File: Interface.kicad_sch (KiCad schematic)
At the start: 32 parts, among them J5601 VBUS_1, J5602 VBUS_2, J5901 SPI, J5902 UART, J5903 Battery_1, J5904 Battery_2, J5905 PV_1, J5906 PV_2, J5907 PV_3, J5908 PV_4, J5909 CH_O_1, J5910 CH_O_2, J5911 CH_O_3, J5912 CH_O_4, J5913 CH_O_5, J5914 CH_O_6, J5915 PV_5, J5916 PV_6, J5917 CH_5V_1, J5918 CH_5V_2, J5919 CH_12V_1, J5920 CH_12V_2

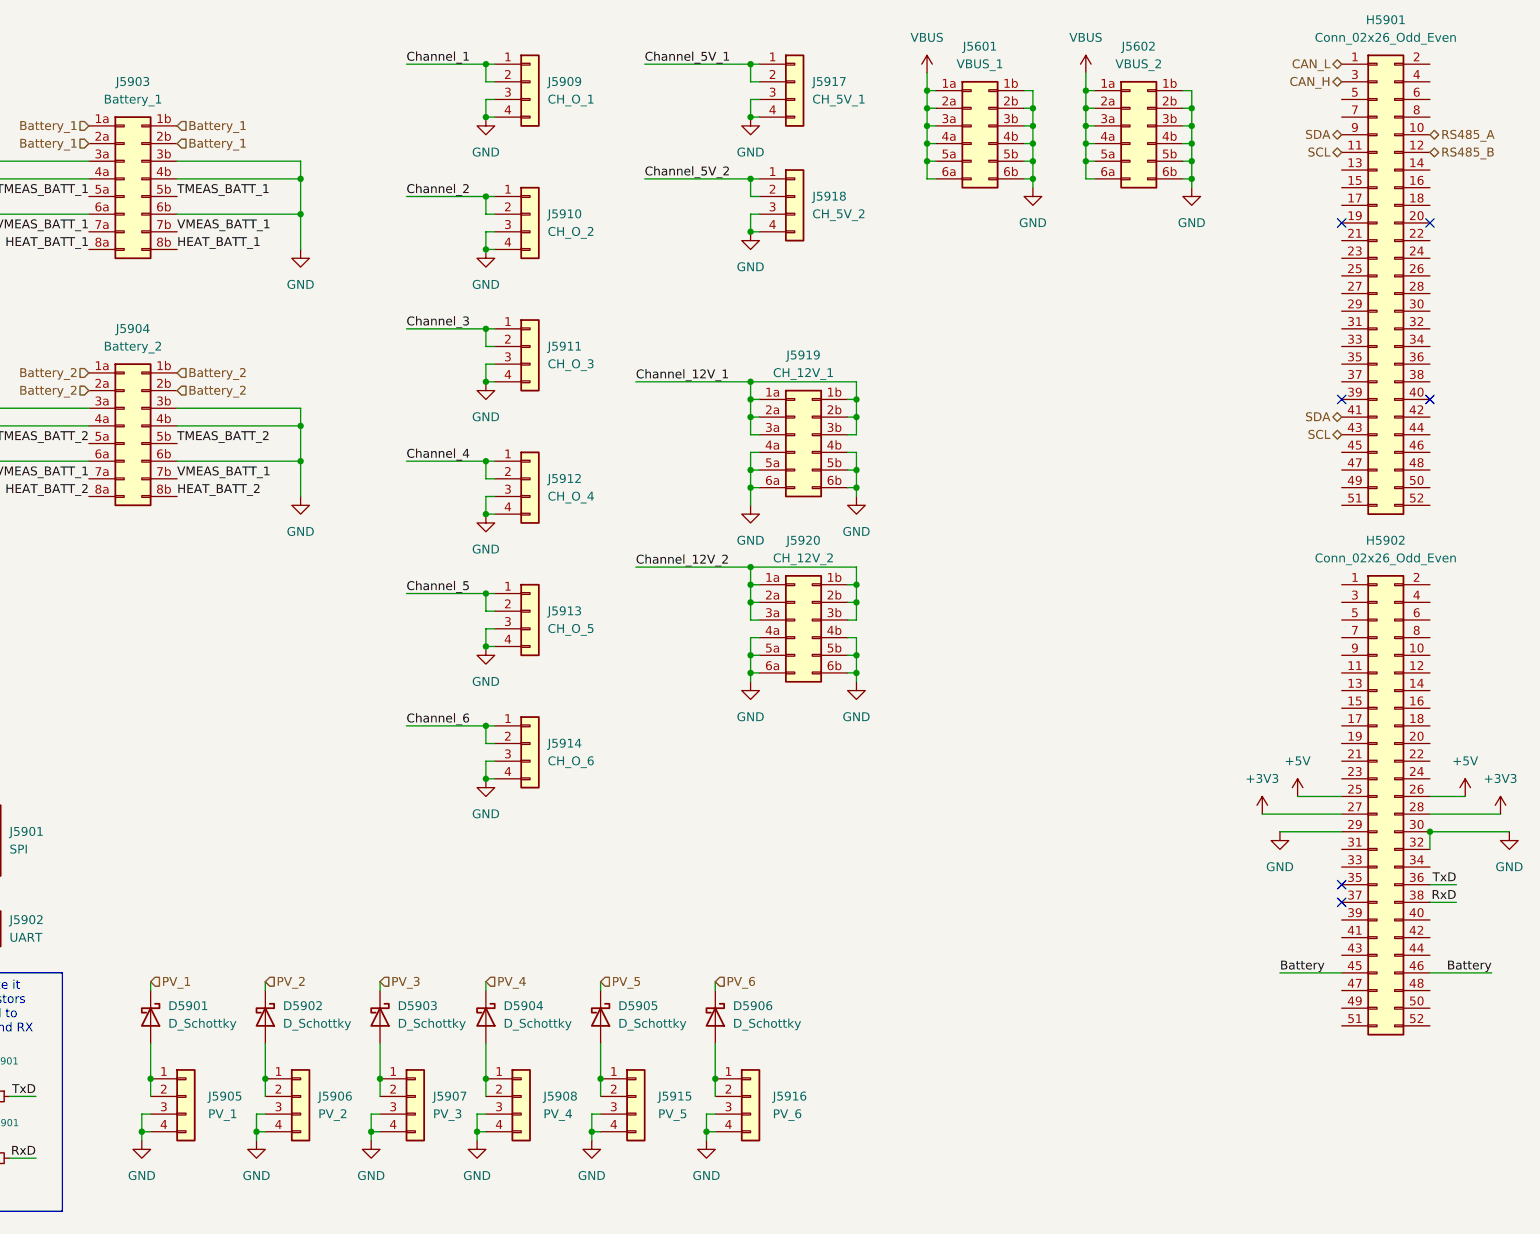
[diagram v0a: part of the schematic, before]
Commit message: added second AMUX and housekeeping
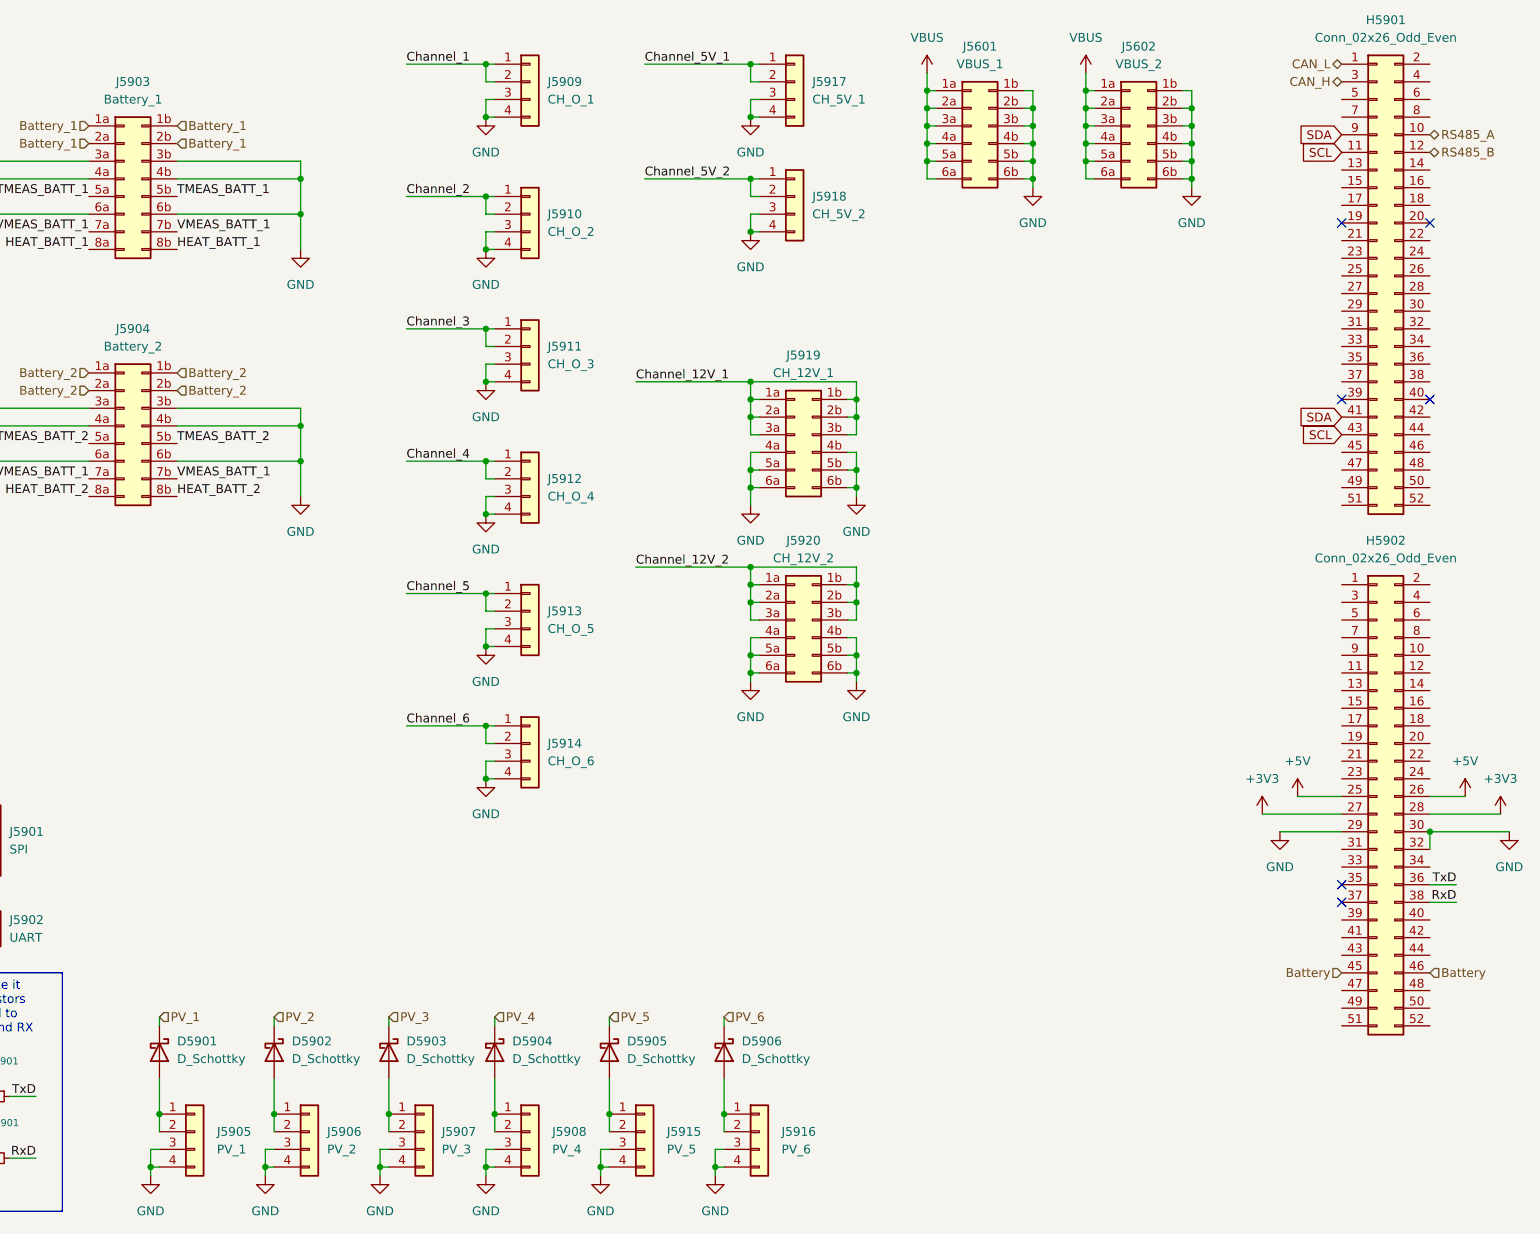
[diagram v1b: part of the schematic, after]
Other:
- moved on the sheet: D5901, D5902, D5903, D5904, D5905, D5906, J5905, J5906, J5907, J5908, J5915, J5916

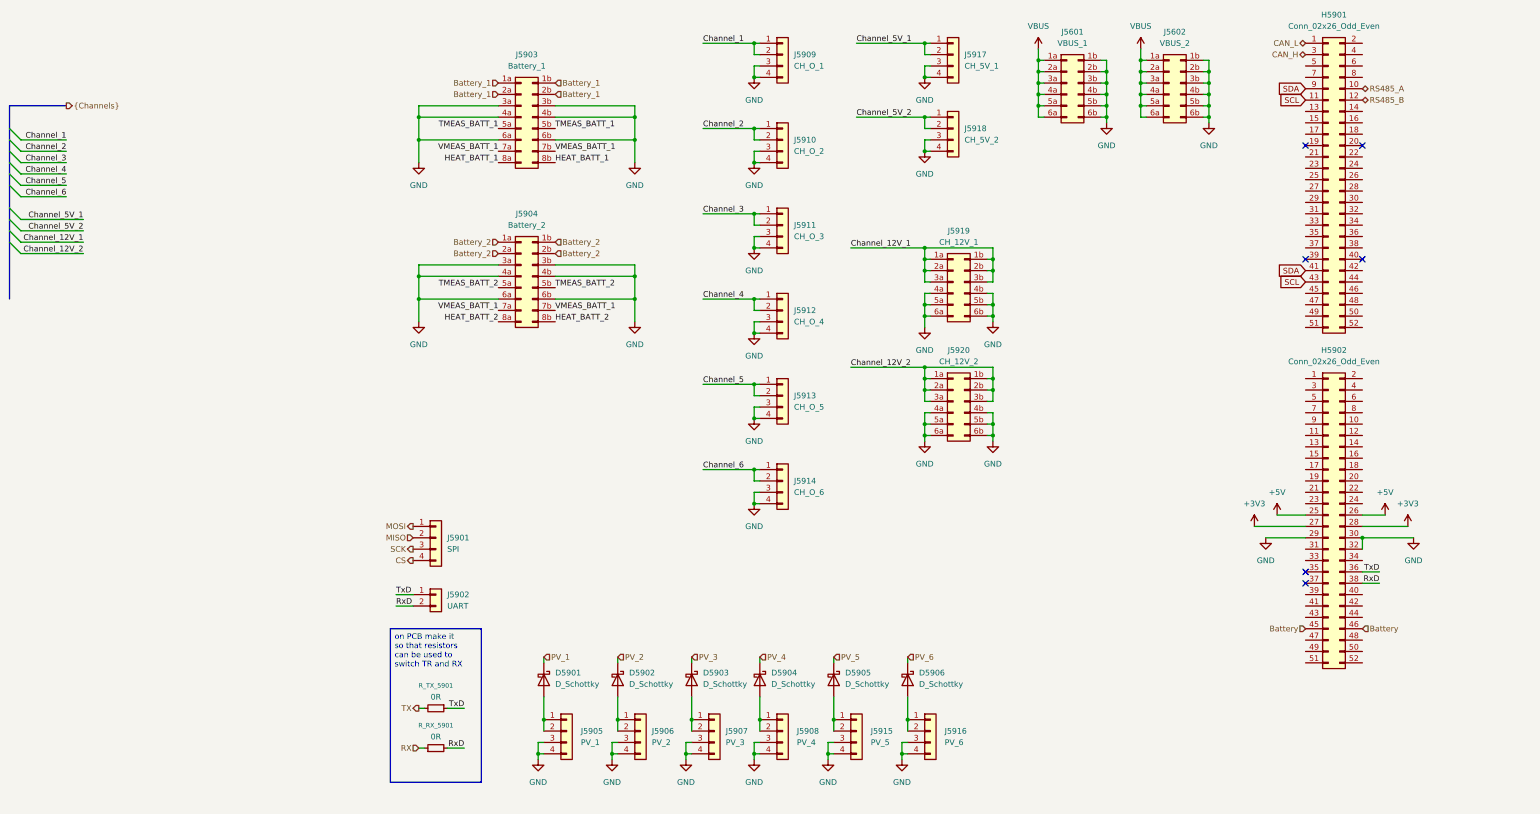
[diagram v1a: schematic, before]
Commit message: added RS422, housekeeping
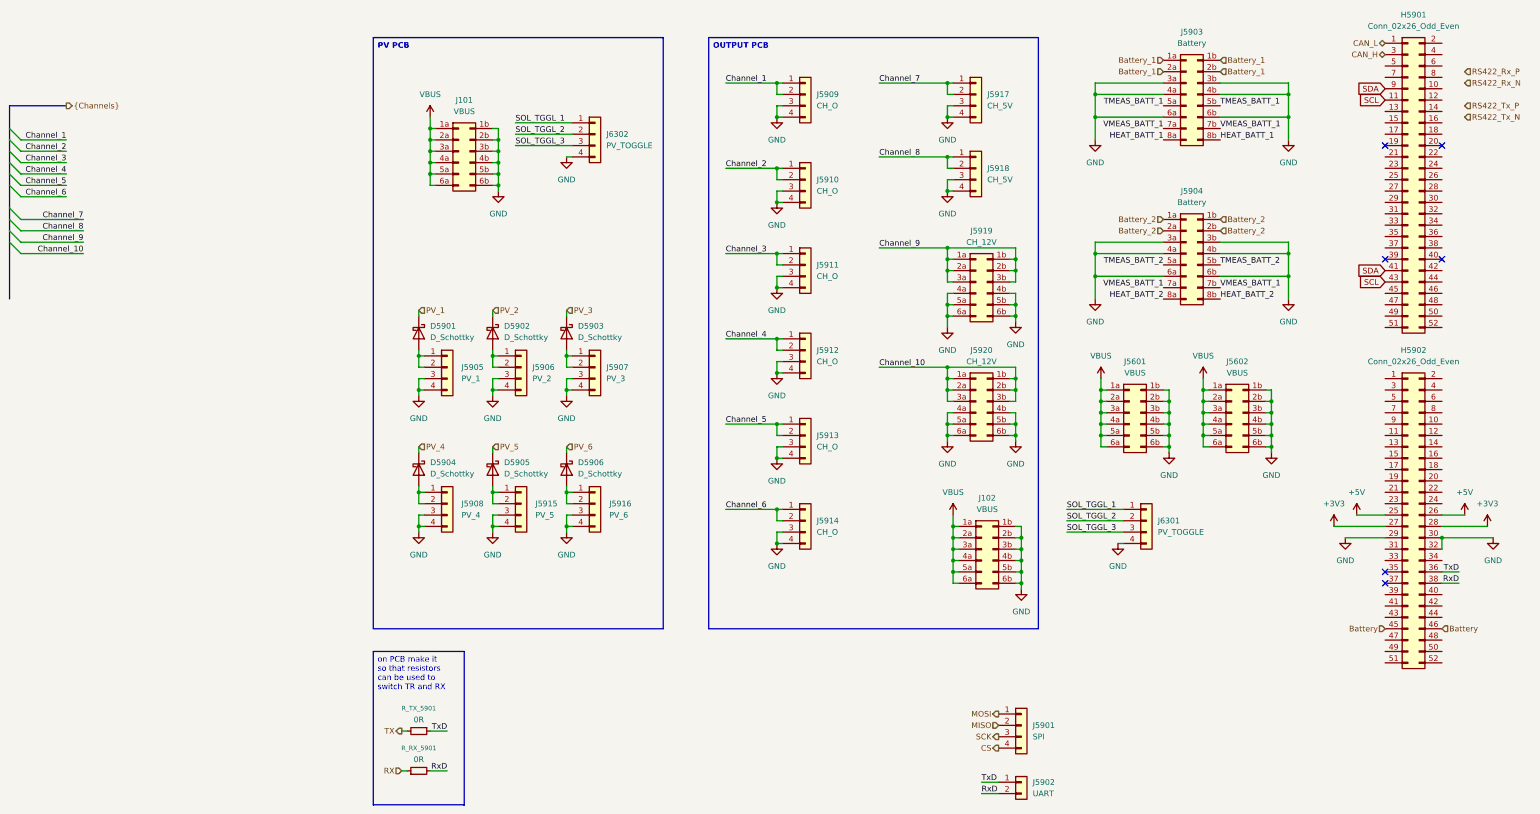
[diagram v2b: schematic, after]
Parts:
- added J101, J102: VBUS, symbol Connector_Generic:Conn_02x06_Row_Letter_Last
- added J6301, J6302: PV_TOGGLE, Connector_Molex:Molex_CLIK-Mate_502494-0470_1x04-1MP_P2.00mm_Horizontal, symbol Connector_Generic:Conn_01x04
- J5601: value VBUS_1 -> VBUS
- J5602: value VBUS_2 -> VBUS
- J5903: value Battery_1 -> Battery
- J5904: value Battery_2 -> Battery
- J5909: value CH_O_1 -> CH_O
- J5910: value CH_O_2 -> CH_O
- J5911: value CH_O_3 -> CH_O
- J5912: value CH_O_4 -> CH_O
- J5913: value CH_O_5 -> CH_O
- J5914: value CH_O_6 -> CH_O
- J5917: value CH_5V_1 -> CH_5V
- J5918: value CH_5V_2 -> CH_5V
- J5919: value CH_12V_1 -> CH_12V
- J5920: value CH_12V_2 -> CH_12V
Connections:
- net GND: now also J101.1b (Pin_1b), J101.2b (Pin_2b), J101.3b (Pin_3b), J101.4b (Pin_4b), J101.5b (Pin_5b), J101.6b (Pin_6b), J102.1b (Pin_1b), J102.2b (Pin_2b), J102.3b (Pin_3b), J102.4b (Pin_4b), J102.5b (Pin_5b), J102.6b (Pin_6b), J6301.4 (Pin_4), J6302.4 (Pin_4)
- net VBUS: now also J101.1a (Pin_1a), J101.2a (Pin_2a), J101.3a (Pin_3a), J101.4a (Pin_4a), J101.5a (Pin_5a), J101.6a (Pin_6a), J102.1a (Pin_1a), J102.2a (Pin_2a), J102.3a (Pin_3a), J102.4a (Pin_4a), J102.5a (Pin_5a), J102.6a (Pin_6a)
- net Channel_12V_1 renamed Channel_9
- net Channel_12V_2 renamed Channel_10
- net Channel_5V_1 renamed Channel_7
- net Channel_5V_2 renamed Channel_8
- net RS485_A: no longer names the net of H5901.10 (Pin_10)
- net RS485_B: no longer names the net of H5901.12 (Pin_12)
- new net SOL_TGGL_1: J6301.1 (Pin_1), J6302.1 (Pin_1)
- new net SOL_TGGL_2: J6301.2 (Pin_2), J6302.2 (Pin_2)
- new net SOL_TGGL_3: J6301.3 (Pin_3), J6302.3 (Pin_3)
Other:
- moved on the sheet: D5901, D5902, D5903, D5904, D5905, D5906, H5901, H5902, J5601, J5602, J5901, J5902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

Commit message: updated battery pack module; updated solar inputs module
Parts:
- removed J6301, J6302: PV_TOGGLE, Connector_Molex:Molex_CLIK-Mate_502494-0470_1x04-1MP_P2.00mm_Horizontal, symbol Connector_Generic:Conn_01x04
- added H6301, H6302, H6303, H6304: PC104, Connector_PinSocket_2.54mm:PinSocket_2x26_P2.54mm_Vertical, symbol Connector_Generic:Conn_02x26_Odd_Even
- added J6322: HEADER_PV, Connector_PinSocket_2.54mm:PinSocket_1x08_P2.54mm_Vertical, symbol Connector:Conn_01x08_Socket
- added J6323: HEADER_PV, Connector_PinHeader_2.54mm:PinHeader_1x08_P2.54mm_Vertical, symbol Connector:Conn_01x08_Pin
- added J6324, J6326: HEADER_CHAN, Connector_PinHeader_2.54mm:PinHeader_1x10_P2.54mm_Vertical, symbol Connector:Conn_01x10_Pin
- added J6325: HEADER_CHAN, symbol Connector:Conn_01x10_Socket
- added J6327: HEADER_CHAN, Connector_PinSocket_2.54mm:PinSocket_1x10_P2.54mm_Vertical, symbol Connector:Conn_01x10_Socket
- H6305: renamed from H5901; value Conn_02x26_Odd_Even -> PC104
- H6306: renamed from H5902; value Conn_02x26_Odd_Even -> PC104
- J6301: renamed from J5905; value PV_1 -> PV
- J6302: renamed from J5908; value PV_4 -> PV
- J6304: renamed from J5906; value PV_2 -> PV
- J6305: renamed from J5915; value PV_5 -> PV
- J6306: renamed from J5907; value PV_3 -> PV
- J6307: renamed from J5916; value PV_6 -> PV
- J6308: renamed from J5909; value CH_O -> Chan
- J6309: renamed from J5910; value CH_O -> Chan
- J6310: renamed from J5911; value CH_O -> Chan
- J6311: renamed from J5912; value CH_O -> Chan
- J6312: renamed from J5913; value CH_O -> Chan
- J6313: renamed from J5914; value CH_O -> Chan
- J6314: renamed from J5917; value CH_5V -> Chan
- J6315: renamed from J5918; value CH_5V -> Chan
- J6316: renamed from J5919; value CH_12V -> Chan_BUS
- J6317: renamed from J5920; value CH_12V -> Chan_BUS
- renumbered D5901 to D6301, D5904 to D6302, D5902 to D6303, D5905 to D6304, D5903 to D6305, D5906 to D6306, J101 to J6303, J102 to J6318, J5601 to J6319, J5903 to J6320, J5904 to J6321, J5602 to J6328, J5901 to J6329, J5902 to J6330, R_RX_5901 to R_RX_6301, R_TX_5901 to R_TX_6301
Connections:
- net +3V3: now also H6302.27 (Pin_27), H6302.28 (Pin_28), H6304.27 (Pin_27), H6304.28 (Pin_28)
- net +5V: now also H6302.25 (Pin_25), H6302.26 (Pin_26), H6304.25 (Pin_25), H6304.26 (Pin_26)
- net Battery: now also H6302.45 (Pin_45), H6302.46 (Pin_46), H6304.45 (Pin_45), H6304.46 (Pin_46)
- net CAN_H: now also H6301.3 (Pin_3), H6303.3 (Pin_3)
- net CAN_L: now also H6301.1 (Pin_1), H6303.1 (Pin_1)
- net Channel_10: now also J6317.4a (Pin_4a), J6317.5a (Pin_5a), J6317.6a (Pin_6a); no longer J6317.1b (Pin_1b), J6317.2b (Pin_2b), J6317.3b (Pin_3b)
- net Channel_9: now also J6316.4a (Pin_4a), J6316.5a (Pin_5a), J6316.6a (Pin_6a); no longer J6316.1b (Pin_1b), J6316.2b (Pin_2b), J6316.3b (Pin_3b)
- net GND: now also J6316.1b (Pin_1b), J6316.2b (Pin_2b), J6316.3b (Pin_3b), J6317.1b (Pin_1b), J6317.2b (Pin_2b), J6317.3b (Pin_3b), H6302.29 (Pin_29), H6302.30 (Pin_30), H6302.32 (Pin_32), H6304.29 (Pin_29), H6304.30 (Pin_30), H6304.32 (Pin_32), J6322.4 (Pin_4), J6322.8 (Pin_8), J6323.4 (Pin_4), J6323.8 (Pin_8), J6324.10 (Pin_10), J6325.10 (Pin_10), J6326.10 (Pin_10), J6327.10 (Pin_10); no longer J6316.4a (Pin_4a), J6316.5a (Pin_5a), J6316.6a (Pin_6a), J6317.4a (Pin_4a), J6317.5a (Pin_5a), J6317.6a (Pin_6a)
- net RxD: now also H6302.38 (Pin_38), H6304.38 (Pin_38)
- net SCL: now also H6301.11 (Pin_11), H6301.43 (Pin_43), H6303.11 (Pin_11), H6303.43 (Pin_43)
- net SDA: now also H6301.41 (Pin_41), H6301.9 (Pin_9), H6303.41 (Pin_41), H6303.9 (Pin_9)
- net SOL_TGGL_1: now also J6322.1 (Pin_1), J6323.1 (Pin_1)
- net SOL_TGGL_2: now also J6322.2 (Pin_2), J6323.2 (Pin_2)
- net SOL_TGGL_3: now also J6322.3 (Pin_3), J6323.3 (Pin_3)
- net TxD: now also H6302.36 (Pin_36), H6304.36 (Pin_36)
- new net Ch_EN_101: J6324.9 (Pin_9), J6325.9 (Pin_9)
- new net Ch_EN_102: J6326.9 (Pin_9), J6327.9 (Pin_9)
- new net Ch_EN_11: J6324.1 (Pin_1), J6325.1 (Pin_1)
- new net Ch_EN_12: J6326.1 (Pin_1), J6327.1 (Pin_1)
- new net Ch_EN_21: J6324.2 (Pin_2), J6325.2 (Pin_2)
- new net Ch_EN_22: J6326.2 (Pin_2), J6327.2 (Pin_2)
- new net Ch_EN_31: J6324.3 (Pin_3), J6325.3 (Pin_3)
- new net Ch_EN_32: J6326.3 (Pin_3), J6327.3 (Pin_3)
- new net Ch_EN_41: J6324.4 (Pin_4), J6325.4 (Pin_4)
- new net Ch_EN_42: J6326.4 (Pin_4), J6327.4 (Pin_4)
- new net Ch_EN_51: J6324.5 (Pin_5), J6325.5 (Pin_5)
- new net Ch_EN_52: J6326.5 (Pin_5), J6327.5 (Pin_5)
- new net Ch_EN_61: J6324.6 (Pin_6), J6325.6 (Pin_6)
- new net Ch_EN_62: J6326.6 (Pin_6), J6327.6 (Pin_6)
- new net Ch_EN_7x: J6324.7 (Pin_7), J6325.7 (Pin_7)
- new net Ch_EN_8x: J6326.7 (Pin_7), J6327.7 (Pin_7)
- new net Ch_EN_91: J6324.8 (Pin_8), J6325.8 (Pin_8)
- new net Ch_EN_92: J6326.8 (Pin_8), J6327.8 (Pin_8)
- new net MPPT_~{EN}: J6322.5 (Pin_5), J6323.5 (Pin_5)
- new net SOL_STAT_1: J6322.6 (Pin_6), J6323.6 (Pin_6)
- new net SOL_STAT_2: J6322.7 (Pin_7), J6323.7 (Pin_7)
- no-connect marks 6 -> 18
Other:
- note added: "OUTPUT PCB"
- note added: "PV PCB"
- moved on the sheet: D6301, D6302, D6303, D6305, D6306, H6305, H6306, J6301, J6302, J6304, J6306, J6307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

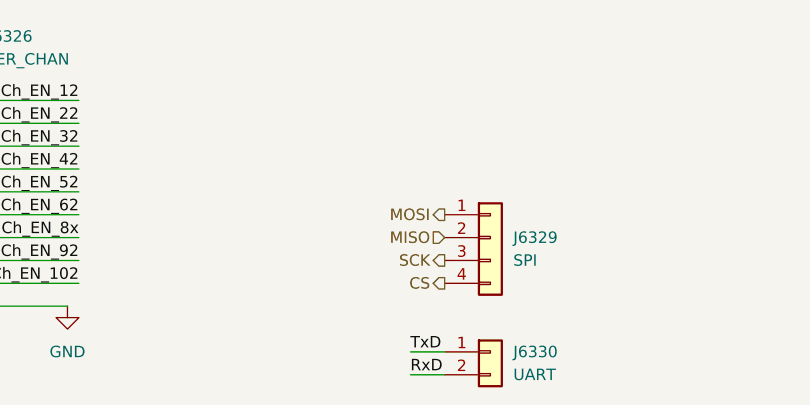
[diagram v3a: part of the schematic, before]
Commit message: added values to most parts
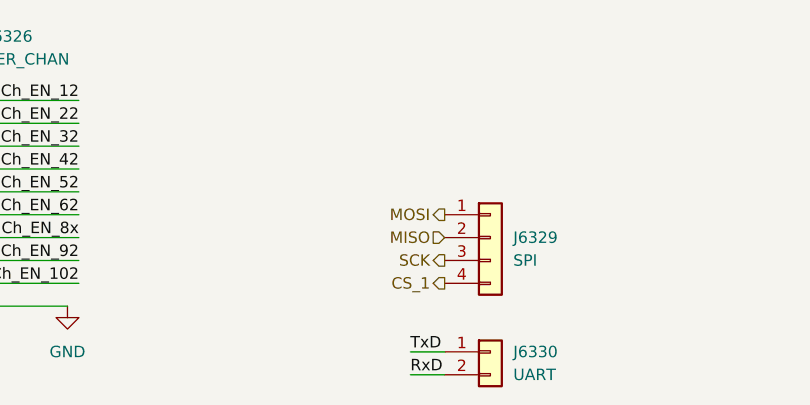
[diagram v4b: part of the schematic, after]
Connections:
- net CS renamed CS_1
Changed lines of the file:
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@@
 		)
 	)
-	(hierarchical_label "CS"
+	(hierarchical_label "CS_1"
 		(shape output)
 		(at 280.67 266.7 180)

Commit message: minor adjustments
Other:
- moved on the sheet: J6316, J6317, J6318

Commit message: wired channel alerts; added schematic for test pbc
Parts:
- added J6331, J801: BATT_PACK, Connector_Harwin:Harwin_Gecko-G125-FVX1605L0X_2x08_P1.25mm_Vertical, symbol Connector_Generic:Conn_02x08_Top_Bottom
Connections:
- net GND: now also J6331.11 (Pin_11), J6331.12 (Pin_12), J6331.14 (Pin_14), J6331.3 (Pin_3), J6331.4 (Pin_4), J6331.6 (Pin_6), J801.11 (Pin_11), J801.12 (Pin_12), J801.14 (Pin_14), J801.3 (Pin_3), J801.4 (Pin_4), J801.6 (Pin_6)
- net HEAT_BATT_1: now also J801.16 (Pin_16), J801.8 (Pin_8)
- net HEAT_BATT_2: now also J6331.16 (Pin_16), J6331.8 (Pin_8)
- net SCL: now also J6320.7b (Pin_7b), J6321.7b (Pin_7b), J6331.15 (Pin_15), J801.15 (Pin_15)
- net SDA: now also J6320.7a (Pin_7a), J6321.7a (Pin_7a), J6331.7 (Pin_7), J801.7 (Pin_7)
- net TMEAS_BATT_1: now also J801.13 (Pin_13), J801.5 (Pin_5)
- net TMEAS_BATT_2: now also J6331.13 (Pin_13), J6331.5 (Pin_5)
- net Battery_1 renamed BATT_PACK_1
- net Battery_2 renamed BATT_PACK_2
- removed net VMEAS_BATT_1: J6320.7a (Pin_7a), J6320.7b (Pin_7b), J6321.7a (Pin_7a), J6321.7b (Pin_7b)
- new net BATTERY_1: J801.1 (Pin_1), J801.10 (Pin_10), J801.2 (Pin_2), J801.9 (Pin_9)
- new net BATTERY_2: J6331.1 (Pin_1), J6331.10 (Pin_10), J6331.2 (Pin_2), J6331.9 (Pin_9)
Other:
- moved on the sheet: D6301, D6302, D6303, D6304, D6305, D6306, J6301, J6302, J6304, J6305, J6306, J6307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
